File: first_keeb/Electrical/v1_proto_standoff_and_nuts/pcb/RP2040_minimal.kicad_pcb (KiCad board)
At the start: 4 copper layers, 67.1 x 66.8 mm, 69 parts, among them J1 Conn_01x04_Socket, P1 USB-TYPE-C-016, Q1 BSS138, SW3 TS-1187A-B-A-B, SW5 TS-1187A-B-A-B, SW6 BUTT1, SW7 BUTT3, SW8 BUTT2, U1 ME6208A44M3G, U2 ME6212C25M5G, U3 PRTR5V0U2X, U5 STM32F401RCTx, U7 SLSS49E, U8 SLSS49E, U9 SLSS49E, Y1 8MHz

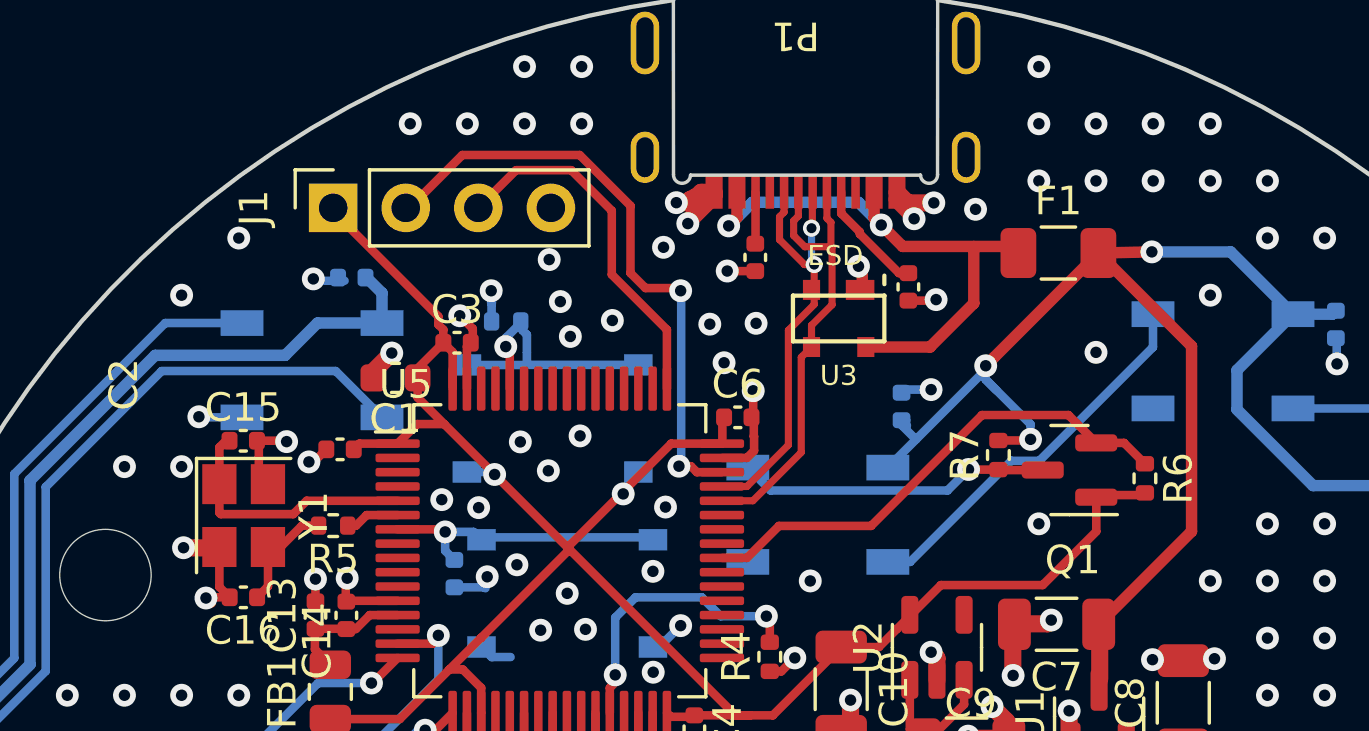
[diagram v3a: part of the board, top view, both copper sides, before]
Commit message: moves pcb components down to make more space, and fixes case
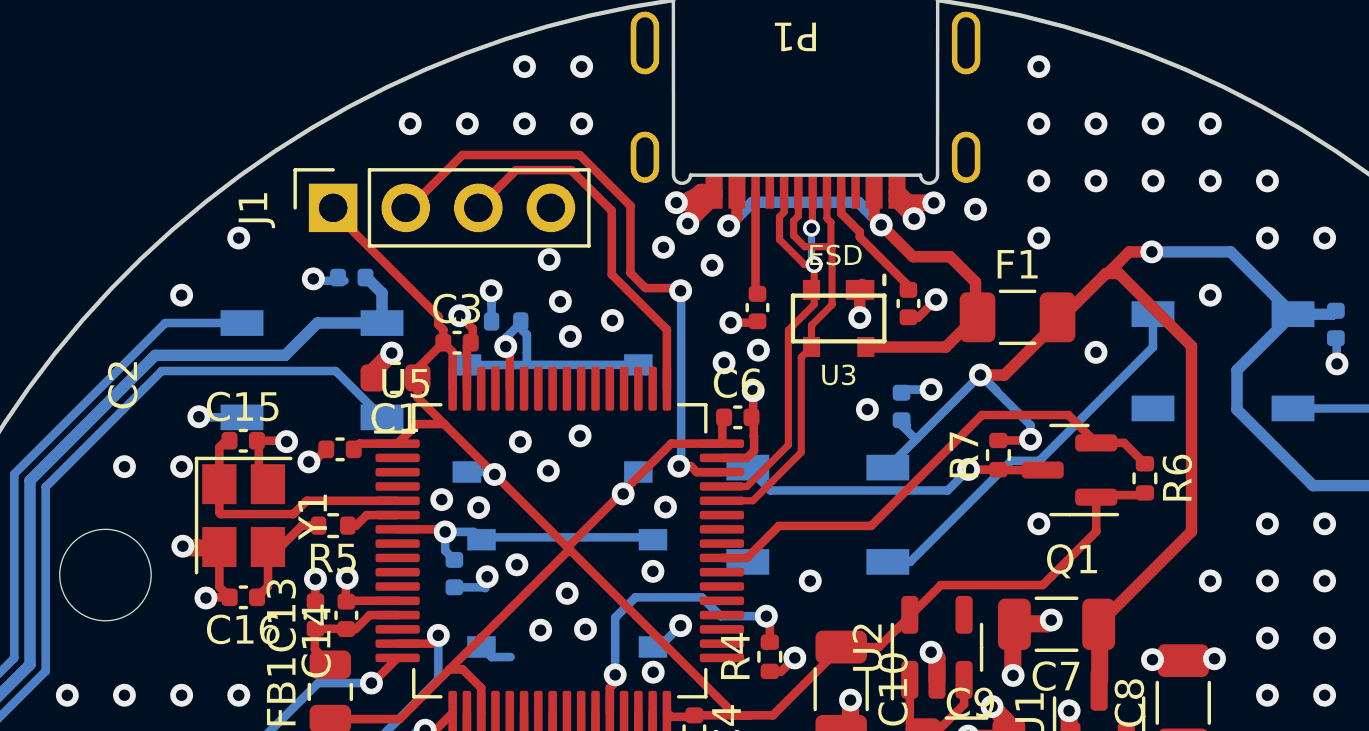
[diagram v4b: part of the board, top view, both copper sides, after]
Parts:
- moved F1 2.67 mm to (107.4, 77.5)
- moved R2 1.76 mm to (98.3, 77.1)
- moved R1 0.59 mm to (103.6, 77.0)
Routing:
- net VBUS: track 21.0 -> 18.6 mm
- net Net-(P1-CC2): track 1.80 -> 3.58 mm
- net GND: track 95.6 -> 96.5 mm, vias 381 -> 383
- net +5V: track 230.2 -> 229.5 mm

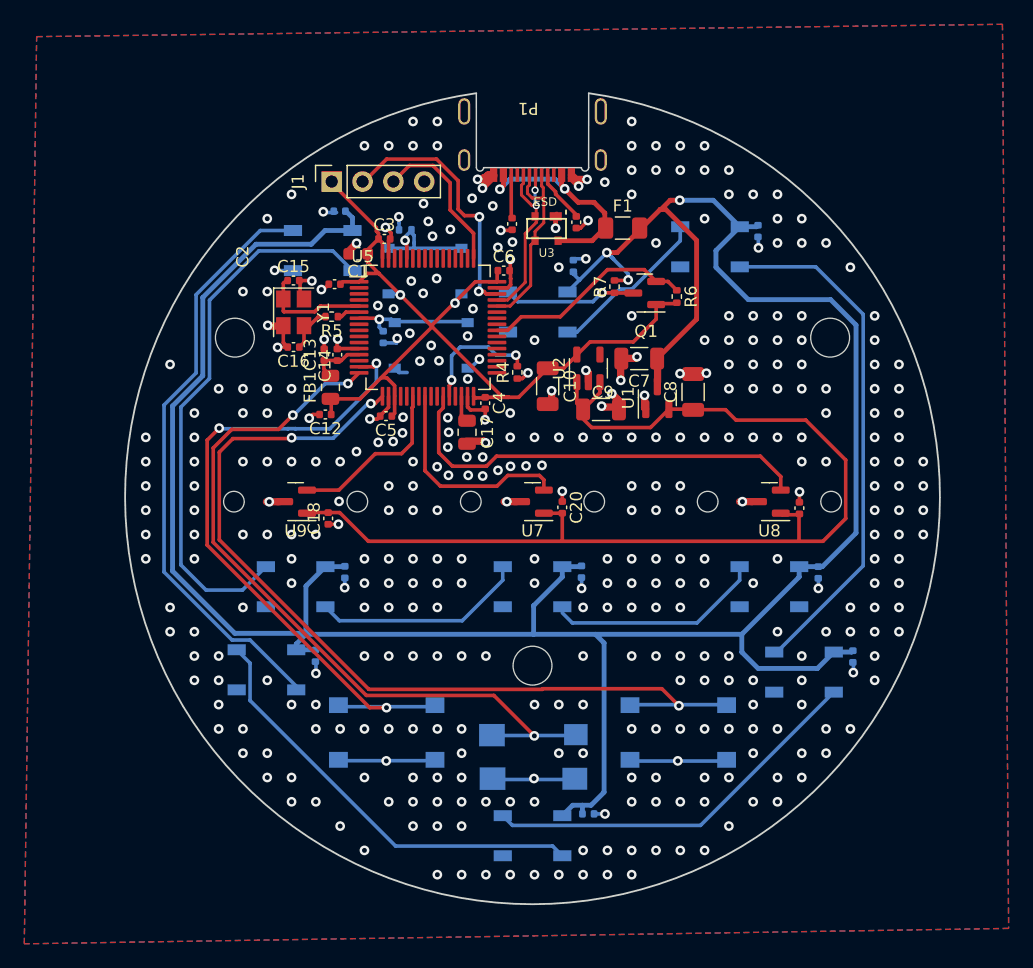
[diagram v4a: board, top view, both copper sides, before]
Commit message: finishes stm with 3d printed standoff holes
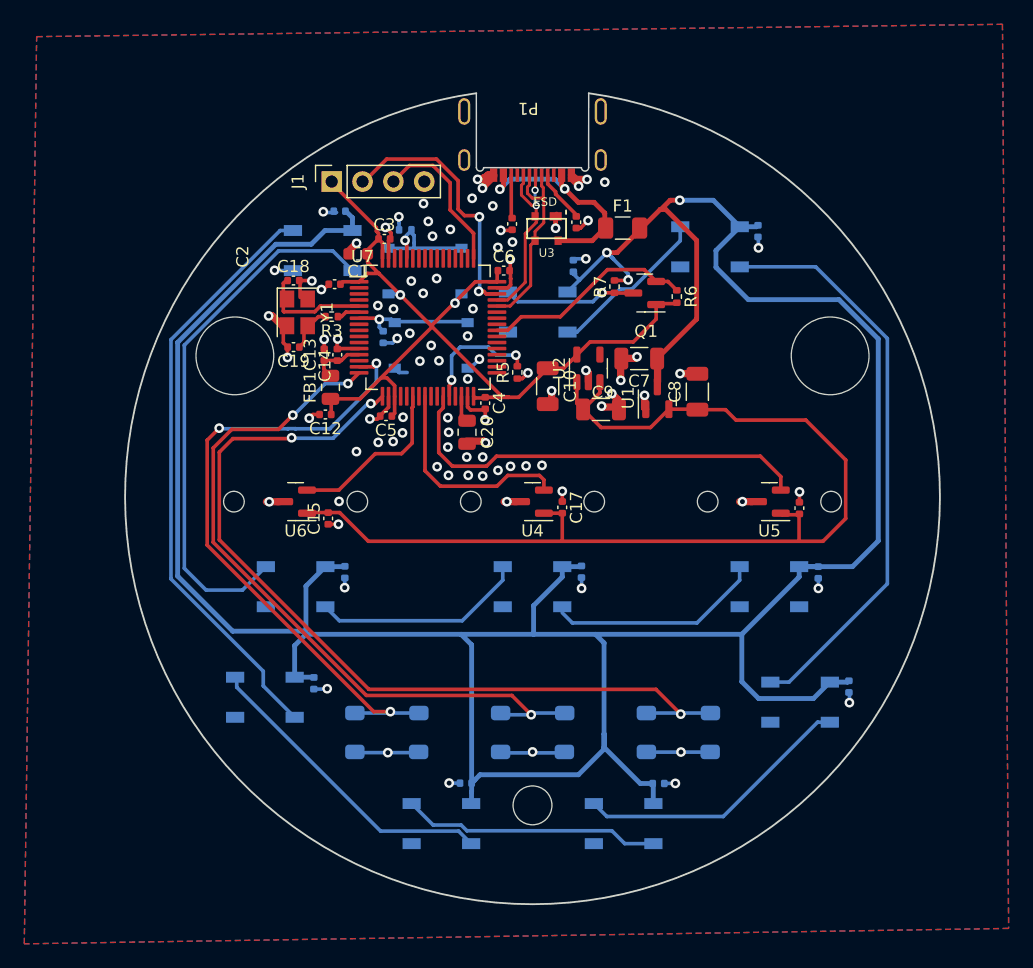
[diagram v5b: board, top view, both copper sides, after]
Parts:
- added C27: 100n, Capacitor_SMD:C_0402_1005Metric, B.Cu at (110.4, 123.2)
- added D7: WS2812B, LED_SMD:LED_WS2812B_PLCC4_5.0x5.0mm_P3.2mm, B.Cu at (107.5, 126.5)
- H1, H2: value MountingHole_3.2mm_M3 -> MountingHole_6.4mm_M6_DIN965; footprint MountingHole:MountingHole_3.2mm_M3 -> MountingHole:MountingHole_6.4mm_M6_DIN965
- H3: value MountingHole_3.2mm_M3 -> MountingHole_3.2mm_M3_DIN965; footprint MountingHole:MountingHole_3.2mm_M3 -> MountingHole:MountingHole_3.2mm_M3_DIN965
- SW3: renamed from SW6; footprint Button_Switch_SMD:SW_Push_1P1T_NO_6x6mm_H9.5mm -> Button_Switch_SMD:PTS647_4.5x4.5mm
- SW4: renamed from SW7; footprint Button_Switch_SMD:SW_Push_1P1T_NO_6x6mm_H9.5mm -> Button_Switch_SMD:PTS647_4.5x4.5mm
- SW5: renamed from SW8; footprint Button_Switch_SMD:SW_Push_1P1T_NO_6x6mm_H9.5mm -> Button_Switch_SMD:PTS647_4.5x4.5mm
- moved H3 11.5 mm to (100.0, 125.0)
- moved C28 10.4 mm to (94.5, 123.2), turned to 180 degrees
- moved D8 7.57 mm to (92.5, 126.5)
- moved C26 2.50 mm to (126.0, 115.2)
- moved D6 2.50 mm to (122.0, 116.5)
- moved C29 2.26 mm to (82.0, 115.0)
- moved D9 2.26 mm to (78.0, 116.1)
- moved SW5 2.00 mm to (100.0, 119.0)
- moved H1 1.50 mm to (124.5, 88.0)
- moved H2 1.50 mm to (75.5, 88.0)
- moved C8 0.35 mm to (113.6, 91.0)
- moved Y1 0.30 mm to (80.6, 84.4)
- renumbered C18 to C15, C19 to C16, C20 to C17, C15 to C18, C16 to C19, C17 to C20, C27 to C28, C28 to C29, C29 to C30, D9 to D10, D7 to D8, D8 to D9, R5 to R3, R3 to R4, R4 to R5, SW3 to SW1, SW5 to SW2, U7 to U4, U8 to U5, U9 to U6, U5 to U7
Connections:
- D8 pad 4: Net-(D6-DOUT) -> Net-(D7-DOUT)
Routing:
- net +5V: track 229.5 -> 263.7 mm
- net Net-(D7-DOUT): track 0.00 -> 21.3 mm
- net Net-(D8-DOUT): track 35.6 -> 25.3 mm
- net Net-(D6-DOUT): track 32.1 -> 23.1 mm
- net GND: track 96.5 -> 88.0 mm, vias 383 -> 92
- net Net-(D5-DOUT): track 42.7 -> 48.0 mm
- net BUTT1: track 63.4 -> 59.8 mm
- net BUTT2: track 74.3 -> 72.0 mm
- net BUTT0: track 56.2 -> 54.0 mm
- net UG_DIN: track 45.5 -> 44.3 mm
